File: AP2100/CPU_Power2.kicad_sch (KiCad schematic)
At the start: 70 parts, among them IC3 AS4C256M16D4-75BCN, IC4 AS4C256M16D4-75BCN, U1 LS1043ASE7KQB

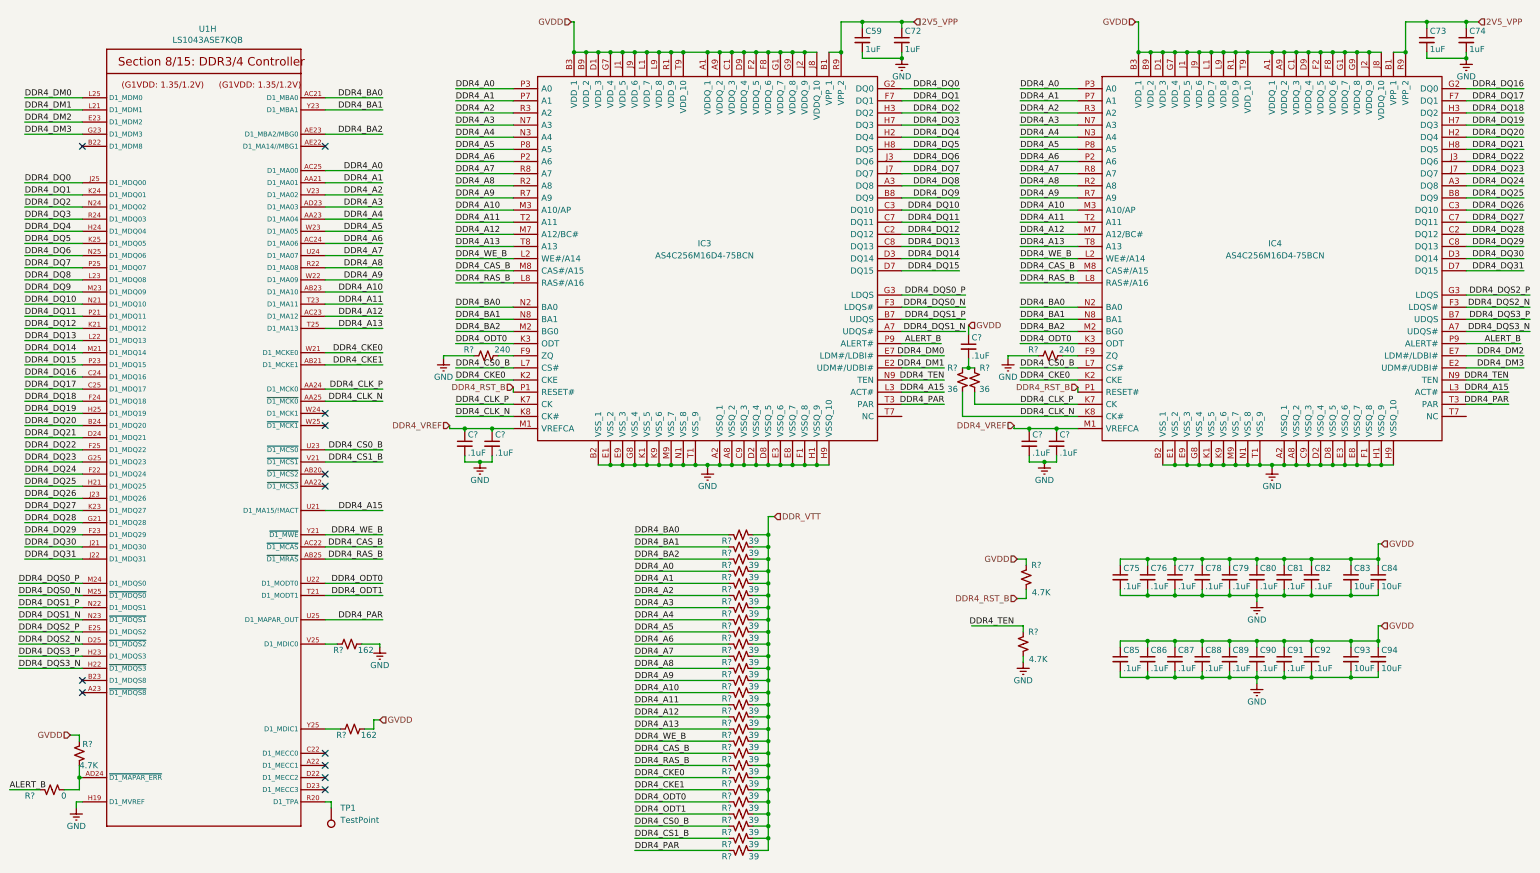
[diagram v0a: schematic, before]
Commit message: Add 2nd CPU power page. Start reset block
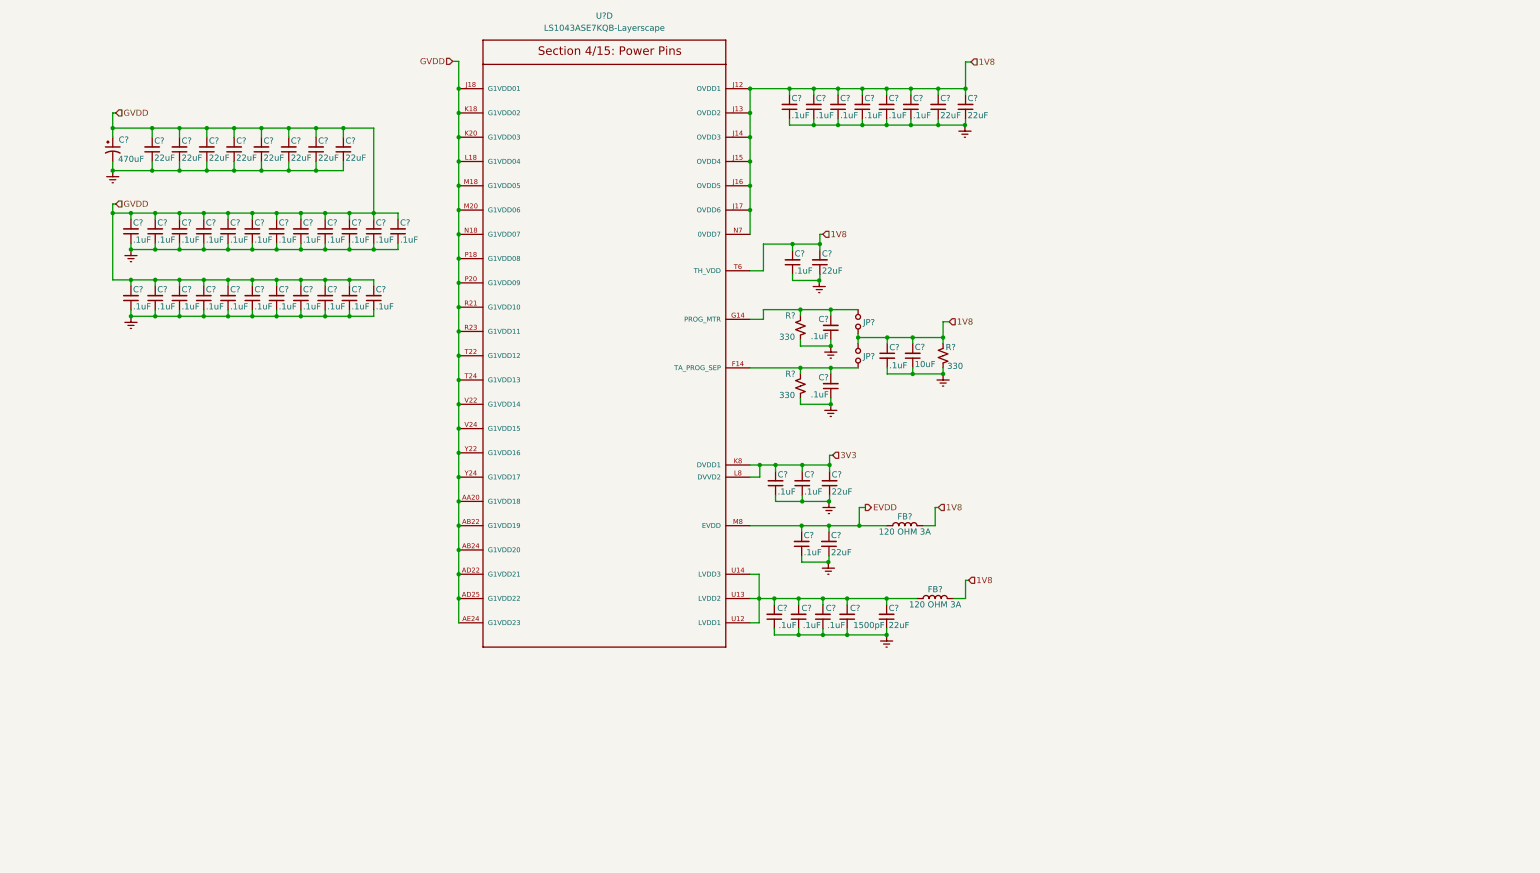
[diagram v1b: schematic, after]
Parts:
- removed C59, C72, C73, C74: 1uF, Capacitor_SMD:C_0402_1005Metric, symbol Device:C_Small
- removed C75, C76, C77, C78, C79, C80, C81, C82, C85, C86, C87, C88, C89, C90, C91, C92, C? (x5): .1uF, Capacitor_SMD:C_0402_1005Metric, symbol Device:C_Small
- removed C83, C84, C93, C94: 10uF, Capacitor_SMD:C_0805_2012Metric, symbol Device:C_Small
- removed IC3, IC4: AS4C256M16D4-75BCN, Scott:BGA96C80P9X16_750X1350X120, symbol Scott:AS4C256M16D4
- removed R? (x27): 39, Resistor_SMD:R_0402_1005Metric, symbol Device:R_Small_US
- removed R? (x2): 36, Resistor_SMD:R_0402_1005Metric, symbol Device:R_Small_US
- removed R? (x2): 240, Resistor_SMD:R_0402_1005Metric, symbol Device:R_Small_US
- removed R? (x3): 4.7K, Resistor_SMD:R_0402_1005Metric, symbol Device:R_Small_US
- removed R?: 0, Resistor_SMD:R_0402_1005Metric, symbol Device:R_Small_US
- removed R? (x2): 162, Resistor_SMD:R_0402_1005Metric, symbol Device:R_Small_US
- removed TP1: TestPoint, symbol Connector:TestPoint
- removed U1: LS1043ASE7KQB, PLS1043ASE7QQA:BGA621C80P25X25_2100X2100X192N, symbol AP2100-rescue:LS1043ASE7KQB-Layerscape
- added C? (x39): .1uF, Capacitor_SMD:C_0201_0603Metric, symbol Device:C_Small
- added C? (x14): 22uF, Capacitor_SMD:C_0805_2012Metric, symbol Device:C_Small
- added C?: 10uF, Capacitor_SMD:C_0805_2012Metric, symbol Device:C_Small
- added C?: 1500pF, Capacitor_SMD:C_0201_0603Metric, symbol Device:C_Small
- added C?: 470uF, Capacitor_SMD:C_Elec_10x10.2, symbol Device:CP1_Small
- added FB? (x2): 120 OHM 3A, Inductor_SMD:L_0603_1608Metric, symbol Device:L
- added JP? (x2): SolderJumper_2_Open, symbol Device:Jumper_NO_Small
- added R? (x3): 330, Resistor_SMD:R_0402_1005Metric, symbol Device:R_Small_US
- added U?: LS1043ASE7KQB-Layerscape, PLS1043ASE7QQA:BGA621C80P25X25_2100X2100X192N, symbol AP2100-rescue:LS1043ASE7KQB-Layerscape
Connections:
- net GND: now also C?.1, C?.1, C?.1, C?.1, C?.1, C?.1, C?.1, C?.1, C?.1, C?.1, C?.1, C?.1, C?.1, C?.1, C?.1, C?.1, C?.1, C?.1, C?.1, C?.1, C?.1, C?.1, C?.1, C?.1, C?.1, C?.1, C?.1, C?.1, C?.1, C?.1, C?.1, C?.1, C?.1, C?.1, C?.1, C?.1, C?.1, C?.1, C?.1, C?.1, C?.1, C?.1, C?.1, C?.1, C?.1, C?.1, C?.1, C?.1, C?.1, C?.1, C?.1, C?.1, C?.1, C?.1, C?.2, C?.2, R?.1, R?.1, R?.2
- net GVDD: now also C?.1, C?.2, C?.2, C?.2, C?.2, C?.2, C?.2, C?.2, C?.2, C?.2, C?.2, C?.2, C?.2, C?.2, C?.2, C?.2, C?.2, C?.2, C?.2, C?.2, C?.2, C?.2, C?.2, C?.2, C?.2, C?.2, C?.2, C?.2, C?.2, C?.2, C?.2, C?.2, U?.AA20 (G1VDD18), U?.AB22 (G1VDD19), U?.AB24 (G1VDD20), U?.AD22 (G1VDD21), U?.AD25 (G1VDD22), U?.AE24 (G1VDD23), U?.J18 (G1VDD01), U?.K18 (G1VDD02), U?.K20 (G1VDD03), U?.L18 (G1VDD04), U?.M18 (G1VDD05), U?.M20 (G1VDD06), U?.N18 (G1VDD07), U?.P18 (G1VDD08), U?.P20 (G1VDD09), U?.R21 (G1VDD10), U?.R23 (G1VDD11), U?.T22 (G1VDD12), U?.T24 (G1VDD13), U?.V22 (G1VDD14), U?.V24 (G1VDD15), U?.Y22 (G1VDD16), U?.Y24 (G1VDD17)
- new net: C?.2, C?.2, C?.2, C?.2, C?.2, FB?.2, U?.U12 (LVDD1), U?.U13 (LVDD2), U?.U14 (LVDD3)
- new net: C?.2, JP?.1, R?.2, U?.F14 (TA_PROG_SEP)
- new net: C?.2, JP?.2, R?.2, U?.G14 (PROG_MTR)
- new net 1V8: C?.1, C?.2, C?.2, C?.2, C?.2, C?.2, C?.2, C?.2, C?.2, C?.2, C?.2, C?.2, FB?.1, FB?.1, JP?.1, JP?.2, R?.1, U?.J12 (OVDD1), U?.J13 (OVDD2), U?.J14 (OVDD3), U?.J15 (OVDD4), U?.J16 (OVDD5), U?.J17 (OVDD6), U?.N7 (0VDD7), U?.T6 (TH_VDD)
- new net 3V3: C?.2, C?.2, C?.2, U?.K8 (DVDD1), U?.L8 (DVVD2)
- new net EVDD: C?.2, C?.2, FB?.2, U?.M8 (EVDD)
- no-connect marks 12 -> 0
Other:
- company: IS ImageStream Internet Solutions, Inc. -> (none)
- title: AP2100 -> (none)
